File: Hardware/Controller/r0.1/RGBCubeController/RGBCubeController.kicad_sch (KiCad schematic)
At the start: 54 parts, among them J1 Conn0, J2 Conn1, J3 Conn2, J4 JTAG, J5 UART, SW1 Reset, SW2 BTN0, SW3 BOOT, SW4 BTN1, U1 ESP32-WROOM-32UE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

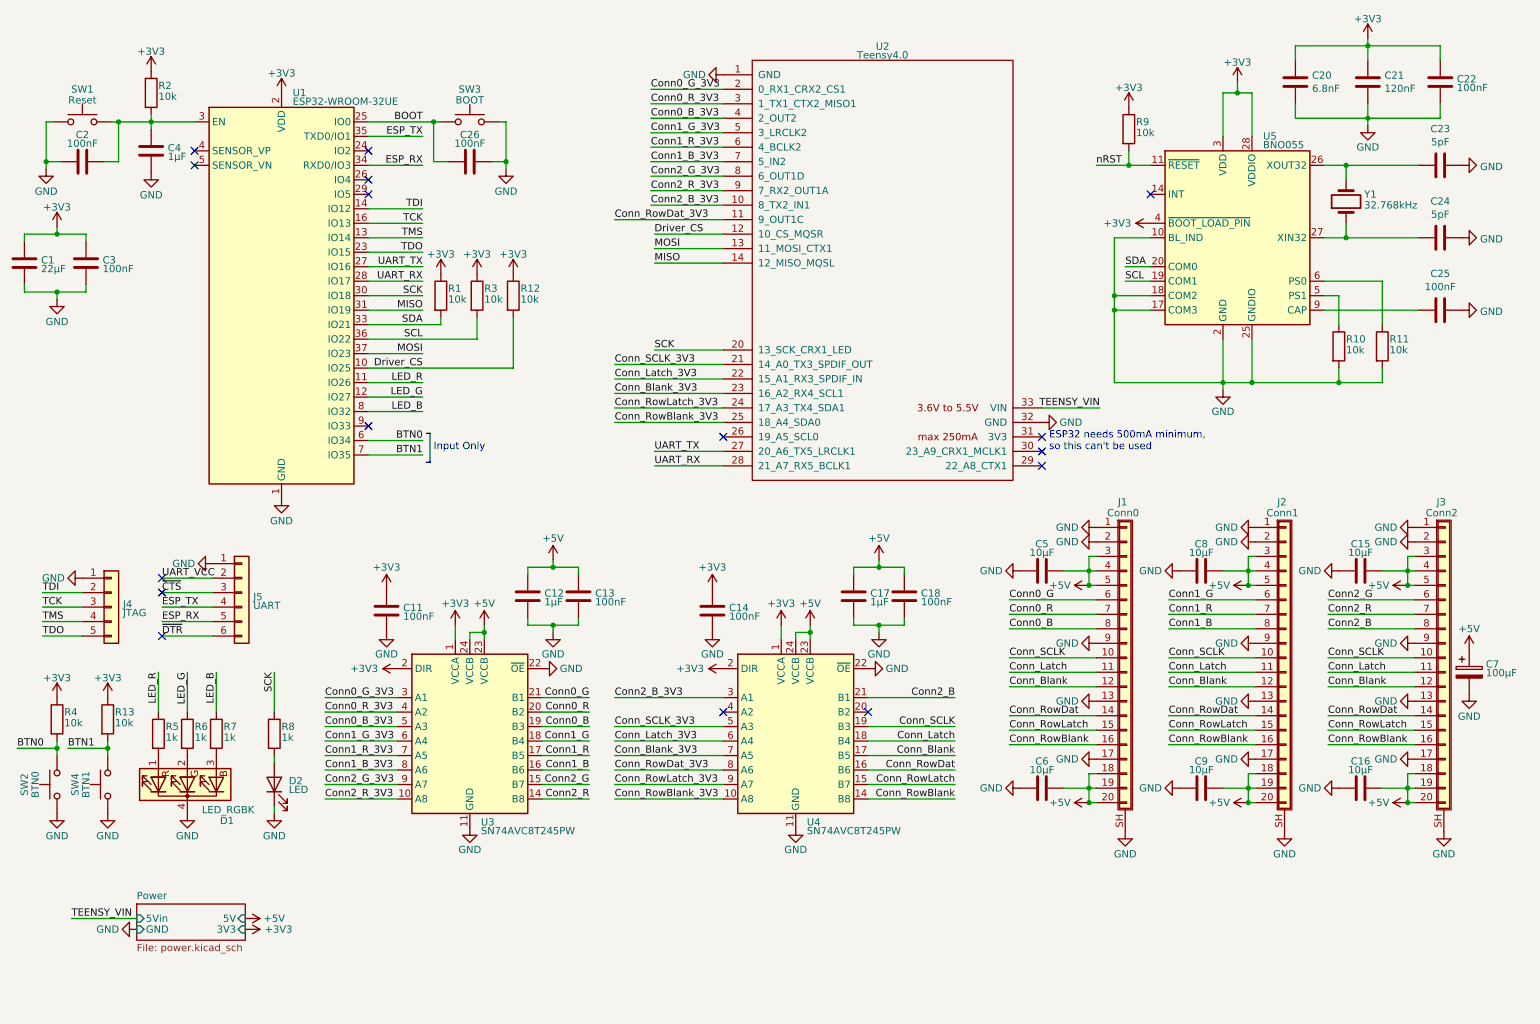
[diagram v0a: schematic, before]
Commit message: [RGBCubeController] Switched to using the Unexpected Maker TinyS3 ESP32 S3 dev board. This removes the need for a 3V3 regulator, reduces the number of components, as well as improving the main microcontroller. It is more expensive, and also takes up more space. Currently parts are all placed on the board (except for the power switch), but no routing has been done.
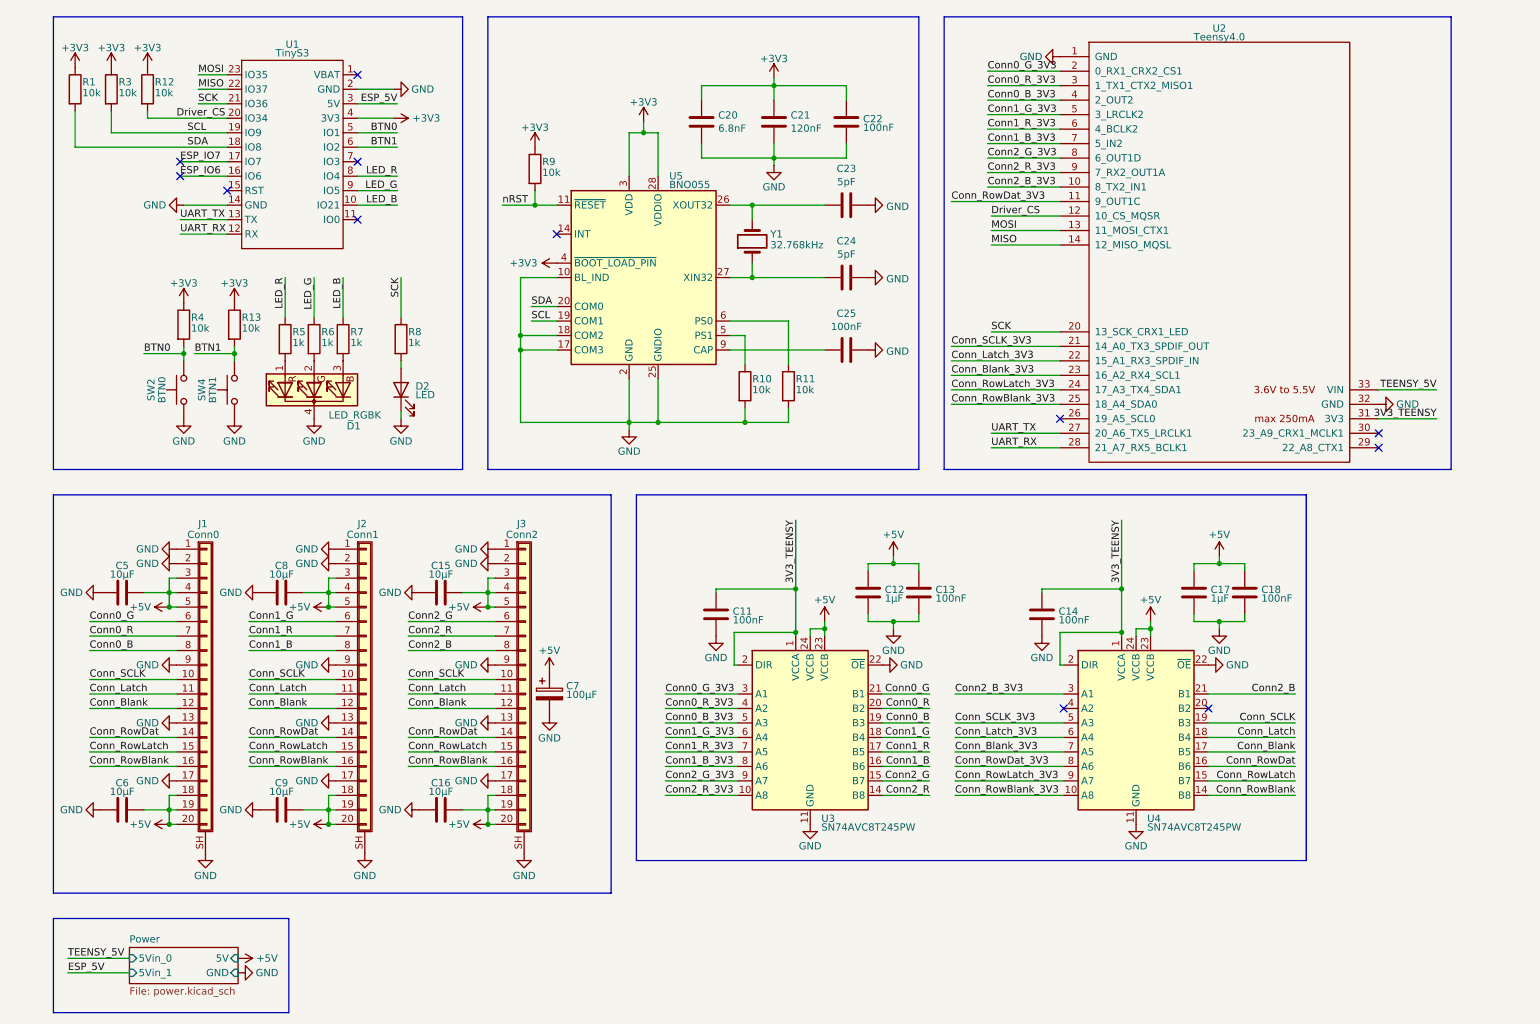
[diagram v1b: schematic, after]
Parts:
- removed C1: 22μF, Capacitor_SMD:C_0603_1608Metric, symbol Device:C
- removed C2, C26, C3: 100nF, Capacitor_SMD:C_0603_1608Metric, symbol Device:C
- removed C4: 1μF, Capacitor_SMD:C_0603_1608Metric, symbol Device:C
- removed J4: JTAG, Connector_PinHeader_2.54mm:PinHeader_1x05_P2.54mm_Vertical, symbol Connector_Generic:Conn_01x05
- removed J5: UART, Connector_PinHeader_2.54mm:PinHeader_1x06_P2.54mm_Horizontal, symbol Connector_Generic:Conn_01x06
- removed R2: 10k, Resistor_SMD:R_0603_1608Metric, symbol Device:R
- removed SW1: Reset, Button_Switch_SMD:SW_SPST_PTS810, symbol Switch:SW_Push
- removed SW3: BOOT, Button_Switch_SMD:SW_SPST_PTS810, symbol Switch:SW_Push
- removed U1: ESP32-WROOM-32UE, RF_Module:ESP32-WROOM-32U, symbol RF_Module:ESP32-WROOM-32U
- added U1: TinyS3, footprints:TinyS3, symbol TinyS3:TinyS3_Symbol
- C23, C24: footprint Capacitor_SMD:C_0603_1608Metric -> Capacitor_SMD:C_0402_1005Metric
- SW2, SW4: footprint Button_Switch_SMD:SW_SPST_PTS810 -> PTS841:PTS841_GKP
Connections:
- net +3V3: now also U1.4 (3V3); no longer C11.1, C14.1, U3.1 (VCCA), U3.2 (DIR), U4.1 (VCCA), U4.2 (DIR)
- net BTN0: now also U1.5 (IO1)
- net BTN1: now also U1.6 (IO2)
- net Driver_CS: now also U1.20 (IO34)
- net GND: now also U1.14 (GND), U1.2 (GND)
- net LED_B: now also U1.10 (IO21)
- net LED_G: now also U1.9 (IO5)
- net LED_R: now also U1.8 (IO4)
- net MISO: now also U1.22 (IO37)
- net MOSI: now also U1.23 (IO35)
- net SCK: now also U1.21 (IO36)
- net SCL: now also U1.19 (IO9)
- net SDA: now also U1.18 (IO8)
- net UART_RX: now also U1.12 (RX)
- net UART_TX: now also U1.13 (TX)
- net 3V3_TEENSY: now reaches U2.31 (3V3)
- net 3V3_TEENSY: now also C11.1, C14.1, U3.1 (VCCA), U3.2 (DIR), U4.1 (VCCA), U4.2 (DIR)
- net TEENSY_VIN renamed TEENSY_5V
- new net ESP_5V: U1.3 (5V)
- new net ESP_IO6: U1.16 (IO6)
- new net ESP_IO7: U1.17 (IO7)
- no-connect marks 16 -> 12
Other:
- sheet Power ports: added 5Vin_0, 5Vin_1; removed 3V3, 5Vin
- note removed: "ESP32 needs 500mA minimum, so this can't be used"
- note removed: "Input Only"
- moved on the sheet: C11, C12, C13, C14, C15, C16, C17, C18, C20, C21, C22, C23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

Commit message: [RGBCubeController] Added Qwiic connector, as well as a pattern to the silkscreen on backside of PCB.
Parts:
- added G1: LOGO, Qwiic:Qwiic, symbol Qwiic:LOGO
- added J4: Qwiic, Connector_JST:JST_SH_SM04B-SRSS-TB_1x04-1MP_P1.00mm_Horizontal, symbol Connector_Generic_MountingPin:Conn_01x04_MountingPin
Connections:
- net +3V3: now also J4.2 (Pin_2)
- net GND: now also J4.1 (Pin_1), J4.MP (MountPin)
- net SCL: now also J4.4 (Pin_4)
- net SDA: now also J4.3 (Pin_3)
